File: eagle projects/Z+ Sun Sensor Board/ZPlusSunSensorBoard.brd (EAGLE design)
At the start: 78 x 78 mm, 51 parts, among them U2 ADS7841E_2K5, U4 LM20BIM7X_NOPB, U6 TLV9051IDCKR, U8 TLV9051IDCKR, U9 TLV9051IDCKR

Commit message: Rev B almost ready
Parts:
- removed A1: SUN_SENSOR_MOUNT, my_library:SUN_SENOR_MASK
- removed C25, C28, C30: 4.7u, rcl:C0805
- removed C26, C29, C31: 0.1u, resistor:C0402
- removed C27, C32, C33: 0.022u, resistor:C0402
- removed DRILEGEND: (no value), drilegend:DRILEGEND
- removed J4, J5, J6: (no value), my_library:2POL254
- removed R13, R19, R7: 3.74k, resistor:R0402
- removed R14, R8: 280R, resistor:R0402
- removed R15: 13.7k, resistor:R0402
- removed TP3, TP6, TP8: TESTPOINT, my_library:TP_P76H50
- removed U6, U9: TLV9051IDCKR, my_library:SC70-5P65_210X110L36X22N_TLV9051
- added C1, C17, C7: 4.7u, rcl:C0805
- added C18, C2, C8: 0.1u, resistor:C0402
- added C23, C3, C9: 0.022u, resistor:C0402
- added R10, R18: 13.7k, resistor:R0402
- added R11, R21, R5: 3.74k, resistor:R0402
- added R17: 280R, resistor:R0402
- added TP10, TP12, TP7: TESTPOINT, my_library:TP_P76H50
- added U$1: SSR_MOUNT_03, my_library:SSR_MOUNT_03
- added U$2, U$3, U$4: (no value), my_library:PHOTODIODE_SILK
- added U1, U5: TSV991AILT, my_library:SOT95P280X145-5N
- R9: value 13.7k -> 280R
- U8: value TLV9051IDCKR -> TSV991AILT; device my_library:SC70-5P65_210X110L36X22N_TLV9051 -> my_library:SOT95P280X145-5N
- moved U8 9.38 mm to (54.3, 36.5), turned to 90 degrees
- moved R1 3.93 mm to (48.6, 49.8)
- moved R3 3.93 mm to (47.3, 49.8)
- moved R9 3.18 mm to (48.6, 43.2), turned to 270 degrees
- moved JP3 1.59 mm to (79.4, 45.4)
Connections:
- removed net N$13: R14.2, R15.1, U9.1
- removed net N$6: R1.2, R3.1, U6.1
- removed net N$9: R8.2, R9.1, U8.1
- new net N$11: C9.1, R11.1, U$1.C2, U5.4
- new net N$14: R10.1, R9.2, U5.3
- new net N$20: R17.2, R18.1, U8.3
- net +3V3: now also C1.1, C17.1, C18.1, C2.1, C7.1, C8.1, R10.2, R18.2, U1.5, U5.5; no longer C25.1, C26.1, C28.1, C29.1, C30.1, C31.1, R15.2, R9.2, U6.5, U9.5
- net 0_DEGREES: now also C3.2, R5.2, TP7.1, U1.1; no longer C27.2, R7.2, TP3.1, U6.4
- net 120_DEGREES: now also C9.2, R11.2, TP10.1, U5.1; no longer C32.2, R13.2, TP6.1, U8.4
- net 240_DEGREES: now also C23.2, R21.2, TP12.1, U8.1; no longer C33.2, R19.2, TP8.1, U9.4
- net GND: now also C1.2, C17.2, C18.2, C2.2, C7.2, C8.2, R17.1, R9.1, U$1.A1, U$1.A2, U$1.A3, U1.2, U5.2; no longer C25.2, C26.2, C28.2, C29.2, C30.2, C31.2, J4.1, J5.1, J6.1, R14.1, R8.1, U6.2, U9.2
- net N$12: now also C23.1, R21.1, U$1.C3, U8.4; no longer C33.1, J4.2, R19.1, U9.3
- net N$3: now also C3.1, R5.1, U$1.C1, U1.4; no longer C27.1, J6.2, R7.1, U6.3
- net N$8: now also R1.2, R3.1, U1.3; no longer C32.1, J5.2, R13.1, U8.3
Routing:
- net +3V3: track 139.6 -> 71.6 mm, vias 0 -> 6
- net N$11: track 0.00 -> 23.2 mm
- net N$3: track 17.8 -> 35.7 mm
- net N$12: track 17.8 -> 33.3 mm
- net N$20: track 0.00 -> 11.2 mm
- net N$14: track 0.00 -> 11.2 mm
- net 240_DEGREES: track 11.9 -> 21.8 mm
- net N$9: track 9.05 -> 0.00 mm
- net N$6: track 9.05 -> 0.00 mm
- net N$13: track 9.05 -> 0.00 mm
- net 120_DEGREES: track 8.66 -> 16.0 mm
- net N$8: track 17.8 -> 11.2 mm
- net 0_DEGREES: track 12.4 -> 15.8 mm
- net UCB0_SPI_MOSI: track 9.48 -> 7.89 mm
- net UCB0_SPI_MISO: track 10.0 -> 8.42 mm
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- added copper zone on layer 15, net +3V4
- added copper zone on layer 15, net +3V6
- added copper zone on layer 15, net +3V8
- added copper zone on layer 2, net GND3
- added copper zone on layer 2, net GND5
- added copper zone on layer 2, net GND7
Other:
- board text added: "Z+ SUN SENSE BOARD - Rev B"
- board text removed: "01-16"
- board text removed: "01-20"
- board text removed: "LAYER-STACK"
- board text removed: "U6"
- board text removed: "U8"
- board text removed: "U9"
- board text removed: "Z+ SUN SENSE BOARD - Rev A"

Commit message: Idk what i changed
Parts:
- moved R4 127.7 mm to (73.0, 50.8)
- moved TP4 11.7 mm to (63.5, 27.9)
- flipped U$2 to the bottom, turned to 60 degrees
- flipped U$3 to the bottom, turned to 180 degrees
- flipped U$4 to the bottom, turned to 300 degrees
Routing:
- net +3V3: track 71.6 -> 129.2 mm, vias 6 -> 10
- net N$2: track 4.25 -> 12.1 mm, vias 0 -> 1
- net GND: track 26.9 -> 29.9 mm, vias 58 -> 60

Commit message: I thinks its done
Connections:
- net GND: now also H1.B3,15, H2.B3,15, H3.B3,15, H4.B3,15
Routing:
- net N$3: track 35.7 -> 33.0 mm
- net +3V3: track 129.2 -> 130.9 mm, vias 10 -> 9
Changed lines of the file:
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@@
 </layers>
 <board>
-<fusionsync huburn="a.YnVzaW5lc3M6bXlkYWwyMA" projecturn="a.YnVzaW5lc3M6bXlkYWwyMCMyMDIxMDExNjM3MjQwMzc3Ng" f3durn="urn:adsk.wipprod:dm.lineage:lyzL_SvwTHSy9JIG63xgXw" pcbguid="" lastpulledtime="" lastsyncedchangeguid="" latestrevisionid="4614a528-9810-4c48-a158-00391c6ed422" lastsyncedrevisionid="4614a528-9810-4c48-a158-00391c6ed422" lastboardhashguid="6c00b5eb-cc7e-dfbf-f6ff-4d714c18001f" lastpushedtime="2021-06-29T00:04:31Z" linktopcb3d="true"/>
+<fusionsync huburn="a.YnVzaW5lc3M6bXlkYWwyMA" projecturn="a.YnVzaW5lc3M6bXlkYWwyMCMyMDIxMDExNjM3MjQwMzc3Ng" f3durn="urn:adsk.wipprod:dm.lineage:lyzL_SvwTHSy9JIG63xgXw" pcbguid="" lastpulledtime="" lastsyncedchangeguid="" latestrevisionid="c9bbda1a-554e-414f-ba3a-c3ea604c3326" lastsyncedrevisionid="c9bbda1a-554e-414f-ba3a-c3ea604c3326" lastboardhashguid="82b992c5-bdea-62cf-29dd-f28af84ac779" lastpushedtime="2021-07-24T18:26:37Z" linktopcb3d="true"/>
 <plain>
 <wire x1="0" y1="0" x2="31.5" y2="0" width="0.1524" layer="48"/>
@@
 <attribute name="SPICEPREFIX" value="C" x="60.6425" y="55.88" size="1.778" layer="27" rot="R270" display="off"/>
 </element>
-<element name="U2" library="my_library" library_urn="urn:adsk.eagle:library:22876504" package="DBQ16" package3d_urn="urn:adsk.eagle:package:23087509/5" value="ADS7841E_2K5" x="69.85" y="45.4025" smashed="yes">
+<element name="U2" library="my_library" library_urn="urn:adsk.eagle:library:22876504" package="DBQ16" package3d_urn="urn:adsk.eagle:package:23087509/6" value="ADS7841E_2K5" x="69.85" y="45.4025" smashed="yes">
 <attribute name="DATASHEET_URL" value="http://www.ti.com/lit/gpn/ADS7841" x="69.85" y="45.4025" size="1.778" layer="27" display="off"/>
 <attribute name="DESCRIPTION" value="12-Bit, 4-Channel Serial Output Sampling Analog-to-Digital Converter" x="69.85" y="45.4025" size="1.778" layer="27" display="off"/>
@@
 <attribute name="NAME" x="72.0725" y="51.7525" size="1.27" layer="25"/>
 </element>
-<element name="U$1" library="my_library" library_urn="urn:adsk.eagle:library:22876504" package="SSR_MOUNT_03" package3d_urn="urn:adsk.eagle:package:29580098/1" value="SSR_MOUNT_03" x="30.33" y="45.4" smashed="yes" rot="MR0"/>
+<element name="U$1" library="my_library" library_urn="urn:adsk.eagle:library:22876504" package="SSR_MOUNT_03" package3d_urn="urn:adsk.eagle:package:29580098/1" override_package3d_urn="urn:adsk.eagle:package:30064049/2" override_package_urn="urn:adsk.eagle:footprint:29580096/1" value="SSR_MOUNT_03" x="30.33" y="45.4" smashed="yes" rot="MR0"/>
 <element name="C1" library="rcl" library_urn="urn:adsk.eagle:library:334" package="C0805" package3d_urn="urn:adsk.eagle:package:23617/2" value="4.7u" x="50.165" y="49.8475" smashed="yes" rot="R270">
 <attribute name="NAME" x="49.53" y="46.0375" size="1.016" layer="25" rot="R90"/>
@@
 <contactref element="C17" pad="1"/>
 <wire x1="50.165" y1="37.4625" x2="50.165" y2="37.465" width="0.2032" layer="1"/>
-<via x="50.165" y="38.7431" extent="1-16" drill="0.35"/>
 <wire x1="50.165" y1="37.465" x2="50.165" y2="38.7431" width="0.2032" layer="1"/>
-<wire x1="47.3075" y1="37.1625" x2="47.3075" y2="38.1" width="0.2032" layer="1"/>
-<via x="47.3075" y="38.1" extent="1-16" drill="0.35"/>
+<wire x1="47.3075" y1="37.1625" x2="47.3075" y2="39.0525" width="0.2032" layer="1"/>
+<via x="47.3075" y="39.0525" extent="1-16" drill="0.35"/>
 <wire x1="51.7525" y1="37.1625" x2="50.4675" y2="37.1625" width="0.2032" layer="1"/>
 <wire x1="50.4675" y1="37.1625" x2="50.165" y2="37.465" width="0.2032" layer="1"/>
@@
 <wire x1="60.453" y1="35.56145" x2="58.02565" y2="33.1341" width="0.2032" layer="1"/>
 <wire x1="58.02565" y1="33.1341" x2="49.88083125" y2="33.1341" width="0.2032" layer="1"/>
-<wire x1="47.3075" y1="38.1" x2="47.3075" y2="38.735" width="0.2032" layer="16"/>
-<wire x1="47.3075" y1="38.735" x2="47.3075" y2="44.7675" width="0.2032" layer="16"/>
+<wire x1="47.3075" y1="39.0525" x2="47.3075" y2="44.7675" width="0.2032" layer="16"/>
 <wire x1="47.3075" y1="44.7675" x2="47.3075" y2="45.4025" width="0.2032" layer="16"/>
 <wire x1="47.3075" y1="45.4025" x2="47.3075" y2="51.435" width="0.2032" layer="16"/>
@@
 <wire x1="50.165" y1="45.4106" x2="48.87156875" y2="45.4106" width="0.2032" layer="16"/>
 <wire x1="48.87156875" y1="45.4106" x2="48.83936875" y2="45.4428" width="0.2032" layer="16"/>
-<wire x1="48.83936875" y1="38.7753" x2="48.87156875" y2="38.7431" width="0.2032" layer="16"/>
-<wire x1="48.87156875" y1="38.7431" x2="50.165" y2="38.7431" width="0.2032" layer="16"/>
-<wire x1="47.3075" y1="38.735" x2="47.3478" y2="38.7753" width="0.2032" layer="16"/>
-<wire x1="47.3478" y1="38.7753" x2="48.83936875" y2="38.7753" width="0.2032" layer="16"/>
-<wire x1="75.565" y1="41.91" x2="73.9775" y2="41.925" width="0" layer="19" extent="1-1"/>
+<wire x1="50.165" y1="38.7431" x2="49.8556" y2="39.0525" width="0.2032" layer="1"/>
+<wire x1="49.8556" y1="39.0525" x2="47.3075" y2="39.0525" width="0.2032" layer="1"/>
+<wire x1="75.565" y1="41.91" x2="73.9925" y2="41.91" width="0.2032" layer="1"/>
+<wire x1="73.9925" y1="41.91" x2="73.9775" y2="41.925" width="0.2032" layer="1"/>
 </signal>
 <signal name="GND">
@@
 <via x="57.15" y="34.29" extent="1-16" drill="0.35"/>
 <via x="64.4525" y="47.625" extent="1-16" drill="0.35"/>
+<contactref element="H1" pad="B3,15"/>
+<contactref element="H2" pad="B3,15"/>
+<contactref element="H3" pad="B3,15"/>
+<contactref element="H4" pad="B3,15"/>
 </signal>
 <signal name="UCB0_SPI_CLK">
@@
 <wire x1="56.8325" y1="50.4975" x2="56.8025" y2="50.4975" width="0.2032" layer="1"/>
 <wire x1="56.8025" y1="50.4975" x2="56.1975" y2="51.1025" width="0.2032" layer="1"/>
-<wire x1="49.89783125" y1="52.705" x2="49.90313125" y2="52.7103" width="0.2032" layer="1"/>
-<wire x1="55.245" y1="51.435" x2="55.245" y2="51.1025" width="0.2032" layer="1"/>
-<wire x1="29.907103125" y1="52.705" x2="49.89783125" y2="52.705" width="0.2032" layer="1"/>
+<wire x1="55.245" y1="51.6209875" x2="55.245" y2="51.1025" width="0.2032" layer="1"/>
 <wire x1="27.03" y1="50.88" x2="28.11105" y2="51.96105" width="0.2032" layer="1"/>
 <wire x1="28.11105" y1="51.96105" x2="29.907103125" y2="52.705" width="0.2032" layer="1" curve="-45"/>
-<wire x1="52.587896875" y1="52.705" x2="49.89783125" y2="52.705" width="0.2032" layer="1"/>
 <wire x1="54.148190625" y1="52.7103" x2="54.9275" y2="52.3875" width="0.2032" layer="1" curve="-45"/>
 <wire x1="54.9275" y1="52.3875" x2="55.245" y2="51.6209875" width="0.2032" layer="1" curve="-45"/>
-<wire x1="55.245" y1="51.6209875" x2="55.245" y2="51.435" width="0.2032" layer="1"/>
+<wire x1="49.89783125" y1="52.705" x2="49.90313125" y2="52.7103" width="0.2032" layer="1"/>
 <wire x1="49.90313125" y1="52.7103" x2="54.148190625" y2="52.7103" width="0.2032" layer="1"/>
+<wire x1="29.907103125" y1="52.705" x2="49.89783125" y2="52.705" width="0.2032" layer="1"/>
 </signal>
 <signal name="N$12">
@@
 <wire x1="56.8325" y1="37.1625" x2="56.8025" y2="37.1625" width="0.2032" layer="1"/>
 <wire x1="56.8025" y1="37.1625" x2="56.1975" y2="37.7675" width="0.2032" layer="1"/>
-<wire x1="55.245" y1="38.1" x2="55.245" y2="37.7675" width="0.2032" layer="1"/>
 <wire x1="27.29405" y1="39.73595" x2="29.090103125" y2="38.992" width="0.2032" layer="1" curve="45"/>
 <wire x1="27.29405" y1="39.73595" x2="27.23" y2="39.8" width="0.2032" layer="1"/>
@@
 <wire x1="45.72" y1="39.37" x2="46.4865125" y2="39.6875" width="0.2032" layer="1" curve="-45"/>
 <wire x1="46.4865125" y1="39.6875" x2="54.1609875" y2="39.6875" width="0.2032" layer="1"/>
-<wire x1="54.1609875" y1="39.6875" x2="54.2925" y2="39.6875" width="0.2032" layer="1"/>
 <wire x1="55.2425" y1="37.7675" x2="55.2425" y2="38.609521875" width="0.2032" layer="1"/>
 <wire x1="55.2425" y1="38.609521875" x2="54.9275" y2="39.37" width="0.2032" layer="1" curve="45"/>
@@
 <signal name="N$8">
 <contactref element="R1" pad="2"/>
-<wire x1="48.925" y1="49.2275" x2="48.9025" y2="49.205" width="0.2032" layer="1"/>
 <wire x1="48.895" y1="49.2125" x2="48.88" y2="49.1975" width="0.2032" layer="1"/>
 <wire x1="48.5775" y1="49.1975" x2="48.88" y2="49.1975" width="0.2032" layer="1"/>
@@
 <signal name="N$14">
 <contactref element="R9" pad="2"/>
-<wire x1="48.925" y1="42.56" x2="48.9025" y2="42.5375" width="0.2032" layer="1"/>
 <wire x1="48.895" y1="42.545" x2="48.88" y2="42.53" width="0.2032" layer="1"/>
 <wire x1="48.5775" y1="42.53" x2="48.88" y2="42.53" width="0.2032" layer="1"/>
@@
 <signal name="N$20">
 <contactref element="R17" pad="2"/>
-<wire x1="48.925" y1="35.8925" x2="48.9025" y2="35.87" width="0.2032" layer="1"/>
-<wire x1="48.895" y1="35.8775" x2="48.88" y2="35.8625" width="0.2032" layer="1"/>
-<wire x1="48.5775" y1="35.8625" x2="48.88" y2="35.8625" width="0.2032" layer="1"/>
-<wire x1="48.895" y1="35.8775" x2="48.9025" y2="35.87" width="0.2032" layer="1"/>
-<wire x1="47.3075" y1="35.8625" x2="48.5775" y2="35.8625" width="0.2032" layer="1"/>
-<wire x1="48.5775" y1="35.8625" x2="48.5775" y2="34.94033125" width="0.2032" layer="1"/>
 <contactref element="U8" pad="3"/>
 <wire x1="50.02813125" y1="33.4897" x2="54.55436875" y2="33.4897" width="0.2032" layer="1"/>
@@
 <wire x1="55.2425" y1="34.17783125" x2="55.2425" y2="35.2575" width="0.2032" layer="1"/>
 <contactref element="R18" pad="1"/>
+<wire x1="47.3075" y1="35.8625" x2="48.5775" y2="35.8625" width="0.2032" layer="1"/>
+<wire x1="48.5775" y1="35.8625" x2="48.5775" y2="34.94033125" width="0.2032" layer="1"/>
 </signal>
 </signals>
@@
 will not be understood (or retained) with this version.
 </note>
+<note version="9.4" severity="warning">
+Since Version 9.4, EAGLE supports the overriding of 3D packages
+in schematics and board files. Those overridden 3d packages
+will not be understood (or retained) with this version.
+</note>

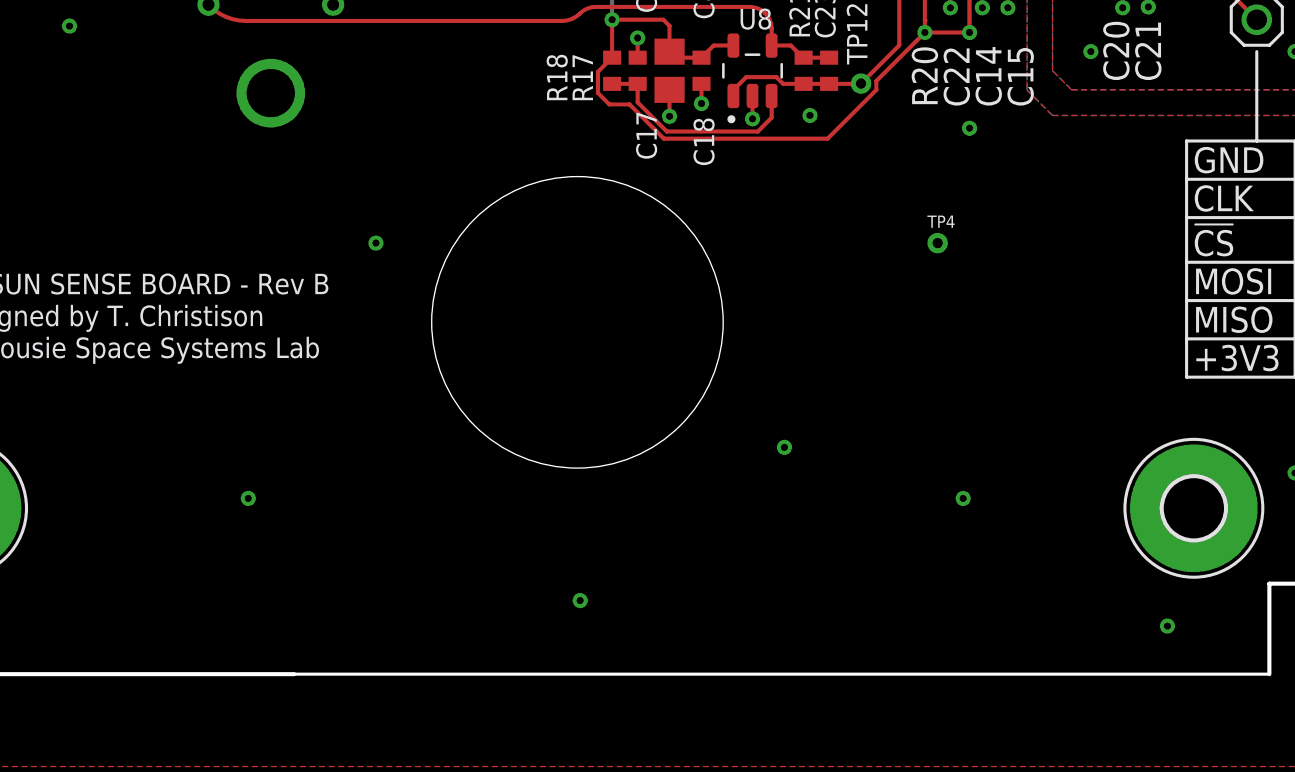
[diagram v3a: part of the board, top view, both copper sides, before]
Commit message: Brandon added burn resistor components
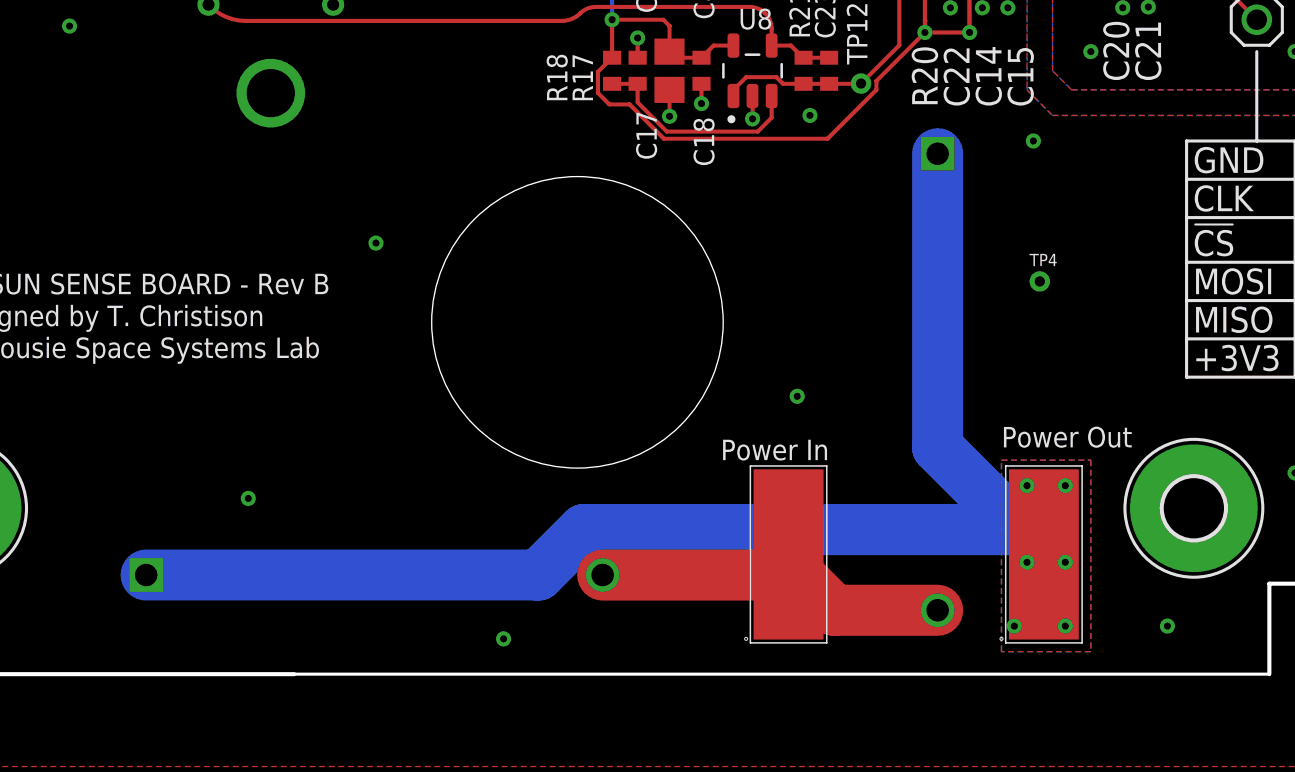
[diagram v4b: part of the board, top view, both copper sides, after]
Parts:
- added J1: Power In, PDUv1:2038638103
- added J2: Power Out, PDUv1:2038638103
- added R6, R7: RS02B2R000FE70, Heating Element:ROX02B_VIS
- moved TP4 5.43 mm to (68.6, 26.0)
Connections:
- new net N$5: J1.P$1, R6.2, R7.2
- new net N$6: J2.P$1, R6.1, R7.1
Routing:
- net N$6: track 0.00 -> 68.2 mm, vias 0 -> 6
- net N$5: track 0.00 -> 18.2 mm
- net GND: vias 60 -> 59
- added copper zone on layer 1, net N$6
- added copper zone on layer 16, net N$6
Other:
- board text added: "Power In"
- board text added: "Power Out"
